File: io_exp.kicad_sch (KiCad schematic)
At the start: 23 parts, among them J26 Conn_01x03, J27 Conn_01x03, J28 Conn_01x03, J4 Conn_01x03, U11 PCF8574ATS

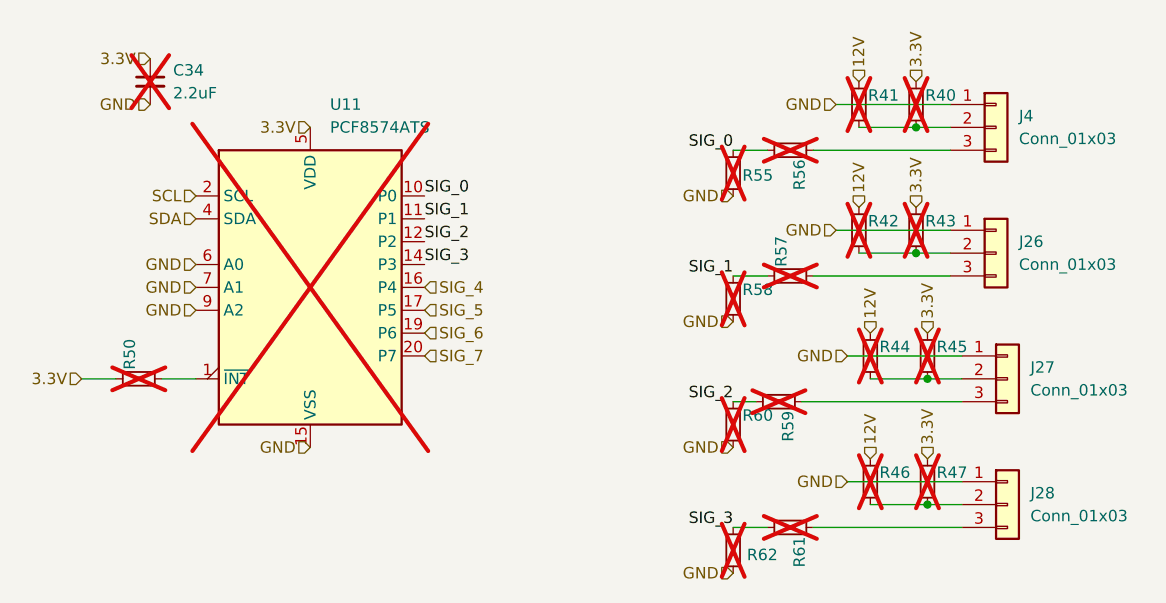
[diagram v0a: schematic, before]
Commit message: fix DNP (was just for checking what was to be bought)
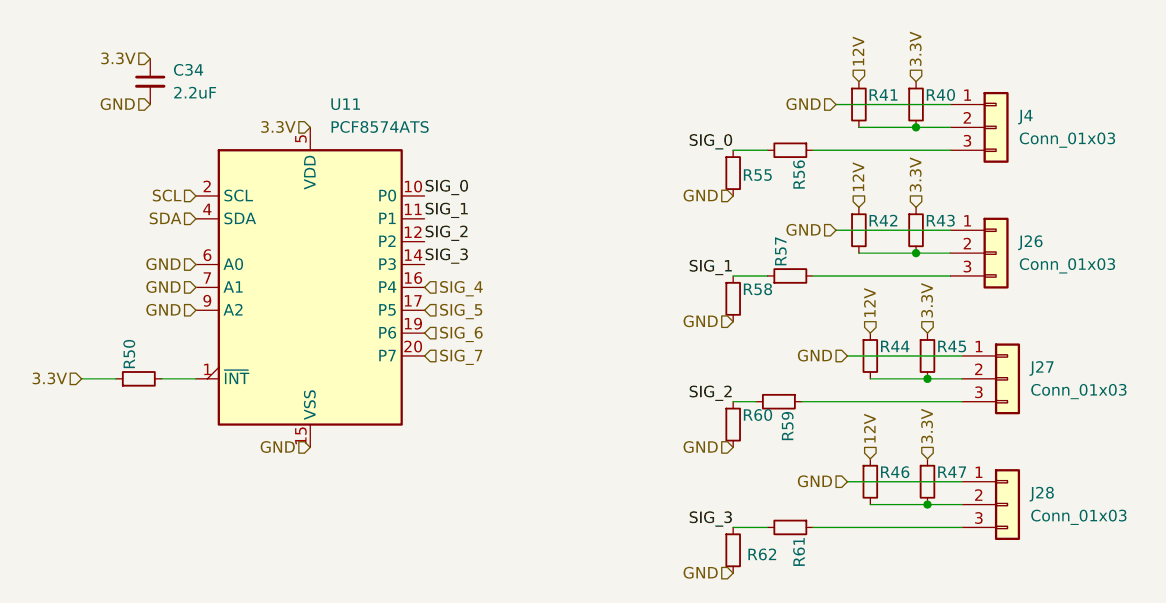
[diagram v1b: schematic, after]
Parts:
- C34, R40, R41, R42, R43, R44, R45, R46, R47, R50, R55, R56, R57, R58, R59, R60, R61, R62, U11: now fitted
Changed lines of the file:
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@@
 		(in_bom yes)
 		(on_board yes)
-		(dnp yes)
+		(dnp no)
 		(property "Reference" "R41"
 			(at 154.686 57.404 0)
@@
 		(in_bom yes)
 		(on_board yes)
-		(dnp yes)
+		(dnp no)
 		(property "Reference" "R46"
 			(at 155.956 99.314 0)
@@
 		(in_bom yes)
 		(on_board yes)
-		(dnp yes)
+		(dnp no)
 		(property "Reference" "R40"
 			(at 161.036 57.404 0)
@@
 		(in_bom yes)
 		(on_board yes)
-		(dnp yes)
+		(dnp no)
 		(property "Reference" "R55"
 			(at 140.716 66.294 0)
@@
 		(in_bom yes)
 		(on_board yes)
-		(dnp yes)
+		(dnp no)
 		(fields_autoplaced yes)
 		(property "Reference" "C34"
@@
 		(in_bom yes)
 		(on_board yes)
-		(dnp yes)
+		(dnp no)
 		(property "Reference" "R56"
 			(at 147.066 64.516 0)
@@
 		(in_bom yes)
 		(on_board yes)
-		(dnp yes)
+		(dnp no)
 		(property "Reference" "R45"
 			(at 162.306 85.344 0)
@@
 		(in_bom yes)
 		(on_board yes)
-		(dnp yes)
+		(dnp no)
 		(property "Reference" "R47"
 			(at 162.306 99.314 0)
@@
 		(in_bom yes)
 		(on_board yes)
-		(dnp yes)
+		(dnp no)
 		(property "Reference" "R59"
 			(at 145.796 92.456 0)
@@
 		(in_bom yes)
 		(on_board yes)
-		(dnp yes)
+		(dnp no)
 		(property "Reference" "R50"
 			(at 72.644 87.884 0)
@@
 		(in_bom yes)
 		(on_board yes)
-		(dnp yes)
+		(dnp no)
 		(fields_autoplaced yes)
 		(property "Reference" "U11"
@@
 		(in_bom yes)
 		(on_board yes)
-		(dnp yes)
+		(dnp no)
 		(property "Reference" "R57"
 			(at 145.034 76.454 0)
@@
 		(in_bom yes)
 		(on_board yes)
-		(dnp yes)
+		(dnp no)
 		(property "Reference" "R60"
 			(at 140.716 92.964 0)
@@
 		(in_bom yes)
 		(on_board yes)
-		(dnp yes)
+		(dnp no)
 		(property "Reference" "R58"
 			(at 140.716 78.994 0)
@@
 		(in_bom yes)
 		(on_board yes)
-		(dnp yes)
+		(dnp no)
 		(property "Reference" "R44"
 			(at 155.956 85.344 0)
@@
 		(in_bom yes)
 		(on_board yes)
-		(dnp yes)
+		(dnp no)
 		(property "Reference" "R43"
 			(at 161.036 71.374 0)
@@
 		(in_bom yes)
 		(on_board yes)
-		(dnp yes)
+		(dnp no)
 		(property "Reference" "R42"
 			(at 154.686 71.374 0)
@@
 		(in_bom yes)
 		(on_board yes)
-		(dnp yes)
+		(dnp no)
 		(property "Reference" "R62"
 			(at 141.224 108.458 0)
@@
 		(in_bom yes)
 		(on_board yes)
-		(dnp yes)
+		(dnp no)
 		(property "Reference" "R61"
 			(at 147.066 106.426 0)

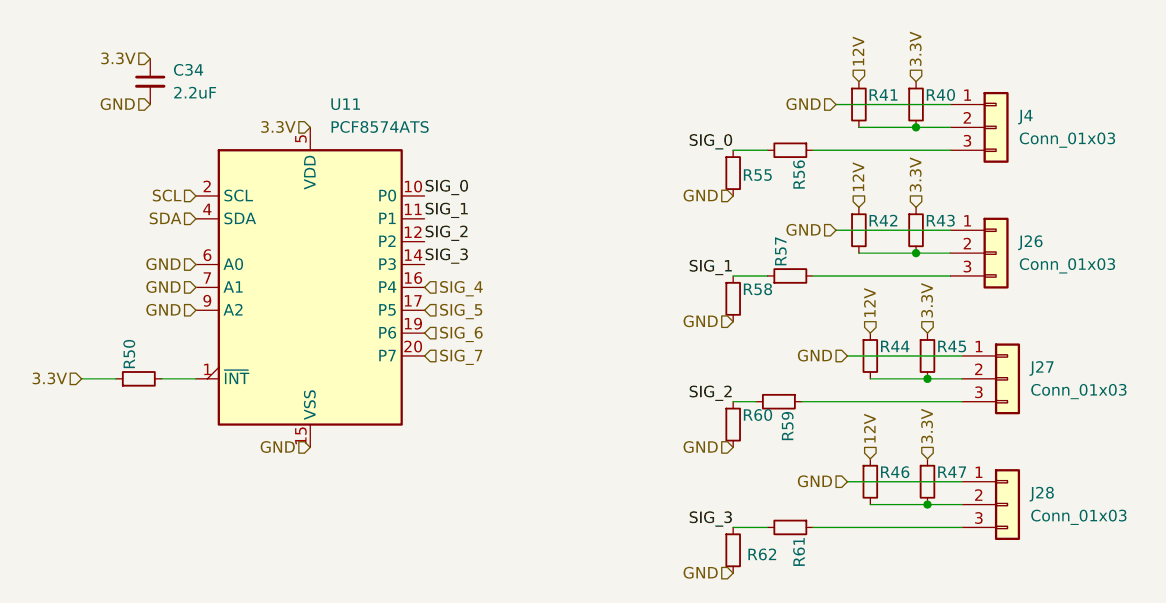
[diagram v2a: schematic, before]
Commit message: fix diodes on transistors + fix warnings
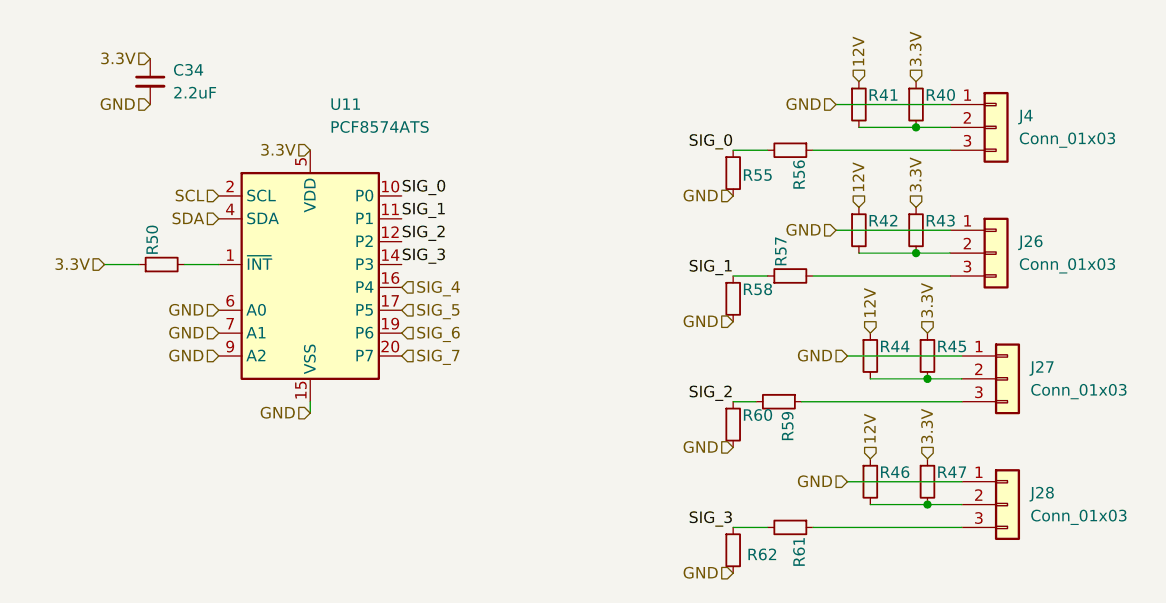
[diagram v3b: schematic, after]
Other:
- moved on the sheet: R50
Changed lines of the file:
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@@
 	(wire
 		(pts
-			(xy 76.2 88.9) (xy 80.01 88.9)
-		)
-		(stroke
-			(width 0)
-			(type default)
-		)
-	)
-	(wire
-		(pts
-			(xy 71.12 88.9) (xy 67.31 88.9)
+			(xy 78.74 76.2) (xy 82.55 76.2)
+		)
+		(stroke
+			(width 0)
+			(type default)
+		)
+	)
+	(wire
+		(pts
+			(xy 73.66 76.2) (xy 69.85 76.2)
 		)
 		(stroke
@@
 		(pts
 			(xy 143.51 63.5) (xy 139.7 63.5)
+		)
+		(stroke
+			(width 0)
+			(type default)
+		)
+	)
+	(wire
+		(pts
+			(xy 92.71 92.71) (xy 92.71 91.44)
 		)
 		(stroke
@@
 	)
 	(label "SIG_1"
-		(at 105.41 71.12 0)
+		(at 102.87 71.12 0)
 		(effects
 			(font
@@
 	)
 	(label "SIG_3"
-		(at 105.41 76.2 0)
+		(at 102.87 76.2 0)
 		(effects
 			(font
@@
 	)
 	(label "SIG_0"
-		(at 105.41 68.58 0)
+		(at 102.87 68.58 0)
 		(effects
 			(font
@@
 	)
 	(label "SIG_2"
-		(at 105.41 73.66 0)
+		(at 102.87 73.66 0)
 		(effects
 			(font
@@
 	(hierarchical_label "GND"
 		(shape input)
-		(at 80.01 78.74 180)
+		(at 82.55 83.82 180)
 		(effects
 			(font
@@
 	(hierarchical_label "GND"
 		(shape input)
-		(at 80.01 81.28 180)
+		(at 82.55 86.36 180)
 		(effects
 			(font
@@
 	(hierarchical_label "SIG_7"
 		(shape input)
-		(at 105.41 86.36 0)
+		(at 102.87 86.36 0)
 		(effects
 			(font
@@
 	(hierarchical_label "SCL"
 		(shape input)
-		(at 80.01 68.58 180)
+		(at 82.55 68.58 180)
 		(effects
 			(font
@@
 	(hierarchical_label "SIG_4"
 		(shape input)
-		(at 105.41 78.74 0)
+		(at 102.87 78.74 0)
 		(effects
 			(font
@@
 	(hierarchical_label "GND"
 		(shape input)
-		(at 80.01 76.2 180)
+		(at 82.55 81.28 180)
 		(effects
 			(font
@@
 	(hierarchical_label "SDA"
 		(shape input)
-		(at 80.01 71.12 180)
+		(at 82.55 71.12 180)
 		(effects
 			(font
@@
 	(hierarchical_label "3.3V"
 		(shape input)
-		(at 92.71 60.96 180)
+		(at 92.71 63.5 180)
 		(effects
 			(font
@@
 	(hierarchical_label "3.3V"
 		(shape input)
-		(at 67.31 88.9 180)
+		(at 69.85 76.2 180)
 		(effects
 			(font
@@
 	(hierarchical_label "SIG_6"
 		(shape input)
-		(at 105.41 83.82 0)
+		(at 102.87 83.82 0)
 		(effects
 			(font
@@
 	(hierarchical_label "SIG_5"
 		(shape input)
-		(at 105.41 81.28 0)
+		(at 102.87 81.28 0)
 		(effects
 			(font
@@
 	(hierarchical_label "GND"
 		(shape input)
-		(at 92.71 96.52 180)
+		(at 92.71 92.71 180)
 		(effects
 			(font
@@
 	(symbol
 		(lib_id "Device:R_Small")
-		(at 73.66 88.9 90)
+		(at 76.2 76.2 90)
 		(unit 1)
 		(body_style 1)
@@
 		(dnp no)
 		(property "Reference" "R50"
-			(at 72.644 87.884 0)
+			(at 75.184 75.184 0)
 			(show_name no)
 			(do_not_autoplace no)
@@
 		)
 		(property "Value" "10kR"
-			(at 74.9299 86.36 0)
+			(at 77.4699 73.66 0)
 			(hide yes)
 			(show_name no)
@@
 		)
 		(property "Footprint" "Resistor_SMD:R_0603_1608Metric"
-			(at 73.66 88.9 0)
+			(at 76.2 76.2 0)
 			(hide yes)
 			(show_name no)
@@
 		)
 		(property "Datasheet" ""
-			(at 73.66 88.9 0)
+			(at 76.2 76.2 0)
 			(hide yes)
 			(show_name no)
@@
 		)
 		(property "Description" "Resistor, small symbol"
-			(at 73.66 88.9 0)
+			(at 76.2 76.2 0)
 			(hide yes)
 			(show_name no)
@@
 		)
 		(property "LCSC#" "C2930027"
-			(at 73.66 88.9 0)
+			(at 76.2 76.2 0)
 			(hide yes)
 			(show_name no)
@@
 			)
 		)
-		(property "Datasheet" "http://www.nxp.com/docs/en/data-sheet/PCF8574_PCF8574A.pdf"
+		(property "Datasheet" "https://www.nxp.com/docs/en/data-sheet/PCF8574_PCF8574A.pdf"
 			(at 92.71 78.74 0)
 			(hide yes)
@@
 			)
 		)
-		(property "Description" "8 Bit Port/Expander to I2C Bus, SSOP-20"
+		(property "Description" "8-bit I/O Expander, I2C interface, interrupt output, fixed address bits 0b0111xxx, SSOP-20"
 			(at 92.71 78.74 0)
 			(hide yes)
